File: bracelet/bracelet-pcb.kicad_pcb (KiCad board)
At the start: 2 copper layers, 65 x 30 mm, 23 parts, among them J1 9V, J2 Treatment Port, J3 Bracelet Enable, U1 AP62250Z6, U2 ESP32-WROOM-32D

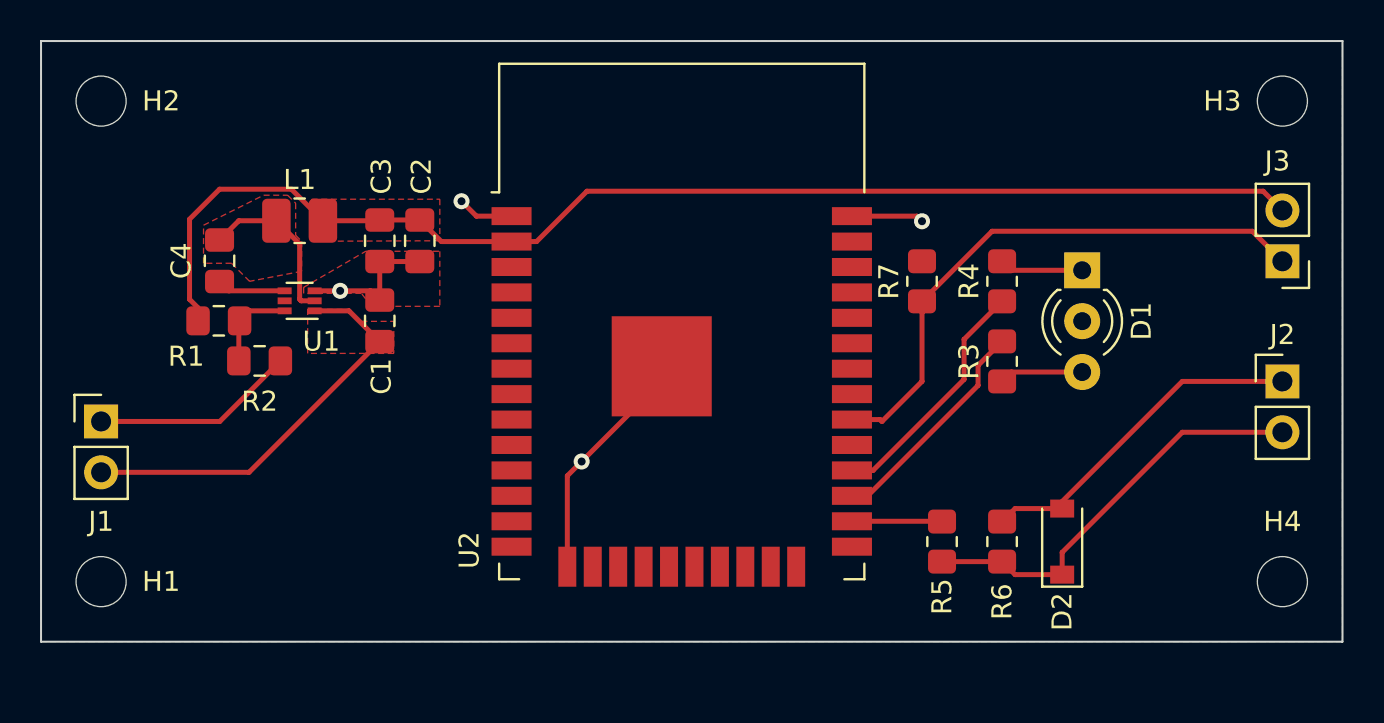
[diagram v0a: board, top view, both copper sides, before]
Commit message: Fix bracelet CHIP_PU, R7 pull down, TSOT26 regulator
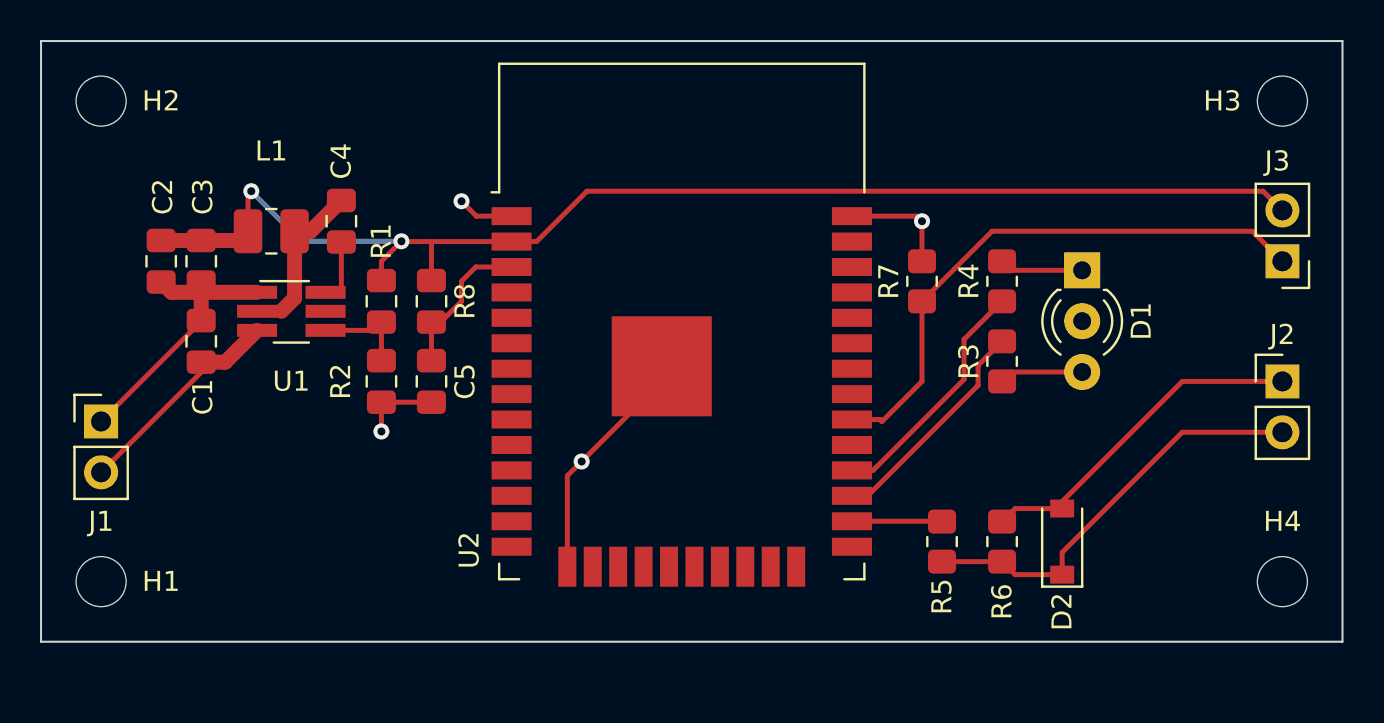
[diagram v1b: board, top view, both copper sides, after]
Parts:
- added C5: 100nF, Capacitor_SMD:C_0805_2012Metric_Pad1.18x1.45mm_HandSolder, F.Cu at (114.5, 117.0)
- added R8: 10k, Capacitor_SMD:C_0805_2012Metric_Pad1.18x1.45mm_HandSolder, F.Cu at (114.5, 113.0)
- U1: value AP62250Z6 -> AP62250WU; footprint Package_TO_SOT_SMD:SOT-563 -> Package_TO_SOT_SMD:TSOT-23-6_HandSoldering
- moved C2 13.0 mm to (101.0, 111.0)
- moved C1 8.97 mm to (103.0, 115.0)
- moved C3 8.97 mm to (103.0, 111.0)
- moved R1 8.18 mm to (112.0, 113.0), turned to -90 degrees
- moved C4 6.40 mm to (110.0, 109.0)
- moved R2 6.17 mm to (112.0, 117.0), turned to -90 degrees
- moved L1 1.51 mm to (106.5, 109.5), turned to 180 degrees
- moved U1 0.67 mm to (107.5, 113.5), turned to 0 degrees
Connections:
- U1 pad 1: +9V -> GND
- U1 pad 3: GND -> +9V
- U1 pad 4: Net-(C4-Pad2) -> Net-(R1-Pad2)
- U1 pad 6: Net-(R1-Pad2) -> Net-(C4-Pad2)
- U2 pad 3: unconnected-(U2-Pad3) -> Net-(U2-Pad3)
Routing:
- net +9V: track 20.5 -> 11.0 mm
- net Net-(U2-Pad3): track 0.00 -> 7.65 mm
- net GND: track 53.1 -> 55.5 mm
- net +3.3V: track 63.0 -> 64.9 mm, vias 0 -> 2
- removed copper zone on F.Cu, net +3.3V
- removed copper zone on F.Cu, net +9V
- removed copper zone on F.Cu, net GND
- removed copper zone on F.Cu, net Net-(C4-Pad1)

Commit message: Reworked board with fixes for v1.1
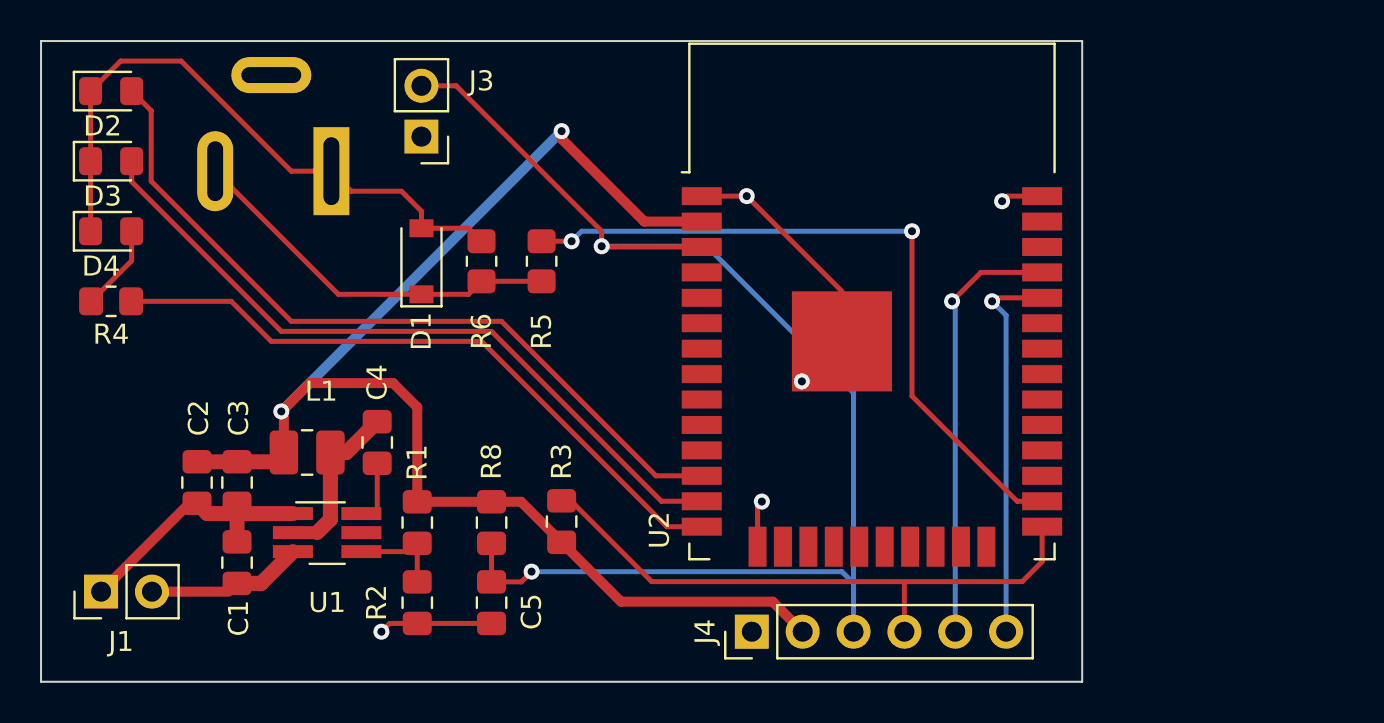
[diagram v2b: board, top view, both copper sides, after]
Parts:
- removed the D1 at (147.0, 111.5)
- removed H1, H2, H3, H4: MountingHole, MountingHole:MountingHole_2.5mm
- removed R7: 1k, Resistor_SMD:R_0805_2012Metric_Pad1.20x1.40mm_HandSolder
- added D2: BLUE, LED_SMD:LED_0805_2012Metric_Pad1.15x1.40mm_HandSolder, F.Cu at (98.5, 102.5)
- added D3: GREEN, LED_SMD:LED_0805_2012Metric_Pad1.15x1.40mm_HandSolder, F.Cu at (98.5, 106.0)
- added D4: RED, LED_SMD:LED_0805_2012Metric_Pad1.15x1.40mm_HandSolder, F.Cu at (98.5, 109.5)
- added J4: Programming Port, Connector_PinHeader_2.54mm:PinHeader_1x06_P2.54mm_Vertical, F.Cu at (130.5, 129.5)
- J1: value 9V -> x3 AAA
- J2: footprint Connector_PinHeader_2.54mm:PinHeader_1x02_P2.54mm_Vertical -> Connector_BarrelJack:BarrelJack_Wuerth_6941xx301002; moved to B.Cu
- R3: value 62 -> 10k; footprint Resistor_SMD:R_0805_2012Metric_Pad1.20x1.40mm_HandSolder -> Capacitor_SMD:C_0805_2012Metric_Pad1.18x1.45mm_HandSolder
- R4: value 62 -> 68
- moved J2 48.6 mm to (109.5, 106.5), turned to 90 degrees
- moved R4 44.5 mm to (98.5, 113.0), turned to 180 degrees
- moved J3 43.4 mm to (114.0, 104.8)
- moved D1 34.9 mm to (114.0, 111.0)
- moved R6 29.5 mm to (117.0, 111.0)
- moved R5 24.4 mm to (120.0, 111.0)
- moved R3 23.4 mm to (121.0, 124.0)
- moved C5 11.5 mm to (117.5, 128.1)
- moved R8 11.4 mm to (117.5, 124.0)
- moved R2 11.2 mm to (113.8, 128.1)
- moved C1 11.2 mm to (104.8, 126.0)
- moved C2 11.2 mm to (102.8, 122.0)
- moved C3 11.2 mm to (104.8, 122.0)
- moved C4 11.2 mm to (111.8, 120.0)
- moved L1 11.2 mm to (108.3, 120.5)
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- renumbered D2 to D1
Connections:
- net +9V renamed +BATT
- net Net-(R5-Pad1) renamed /treatment_port
- C5 pad 1: Net-(U2-Pad3) -> /CHIP_PU
- J3 pad 1: Net-(J3-Pad1) -> GND
- J3 pad 2: +3.3V -> /CHIP_PU
- R3 pad 1: Net-(D1-Pad3) -> +3.3V
- R3 pad 2: Net-(R3-Pad2) -> /IO0
- R4 pad 1: Net-(R4-Pad1) -> /red_led
- R8 pad 2: Net-(U2-Pad3) -> /CHIP_PU
- U2 pad 12: unconnected-(U2-Pad12) -> /blue_led
- U2 pad 13: unconnected-(U2-Pad13) -> /green_led
- U2 pad 14: unconnected-(U2-Pad14) -> /red_led
- U2 pad 25: unconnected-(U2-Pad25) -> /IO0
- U2 pad 27: Net-(R3-Pad2) -> unconnected-(U2-Pad27)
- U2 pad 28: Net-(R4-Pad1) -> unconnected-(U2-Pad28)
- U2 pad 3: Net-(U2-Pad3) -> /CHIP_PU
- U2 pad 30: Net-(J3-Pad1) -> unconnected-(U2-Pad30)
- U2 pad 34: unconnected-(U2-Pad34) -> /RX
- U2 pad 35: unconnected-(U2-Pad35) -> /TX
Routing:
- net /CHIP_PU: track 0.00 -> 65.8 mm, vias 0 -> 2
- net /blue_led: track 0.00 -> 38.5 mm
- net /green_led: track 0.00 -> 36.1 mm
- net /red_led: track 0.00 -> 33.2 mm
- net /treatment_port: track 4.51 -> 35.6 mm, vias 0 -> 2
- net /IO0: track 0.00 -> 30.2 mm
- net Net-(J3-Pad1): track 28.4 -> 0.00 mm
- net /TX: track 0.00 -> 21.7 mm, vias 0 -> 1
- net /RX: track 0.00 -> 19.4 mm, vias 0 -> 1
- net Net-(R4-Pad1): track 12.2 -> 0.00 mm
- net Net-(R3-Pad2): track 11.3 -> 0.00 mm
- net GND: track 55.5 -> 64.0 mm, vias 4 -> 5
- net Net-(U2-Pad3): track 7.65 -> 0.00 mm
- net +3.3V: track 64.9 -> 70.1 mm
- net Net-(D1-Pad3): track 4.19 -> 0.00 mm
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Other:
- board size 65 x 30 mm -> 52 x 32 mm
